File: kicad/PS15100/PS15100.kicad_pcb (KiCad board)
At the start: 2 copper layers, 22 parts

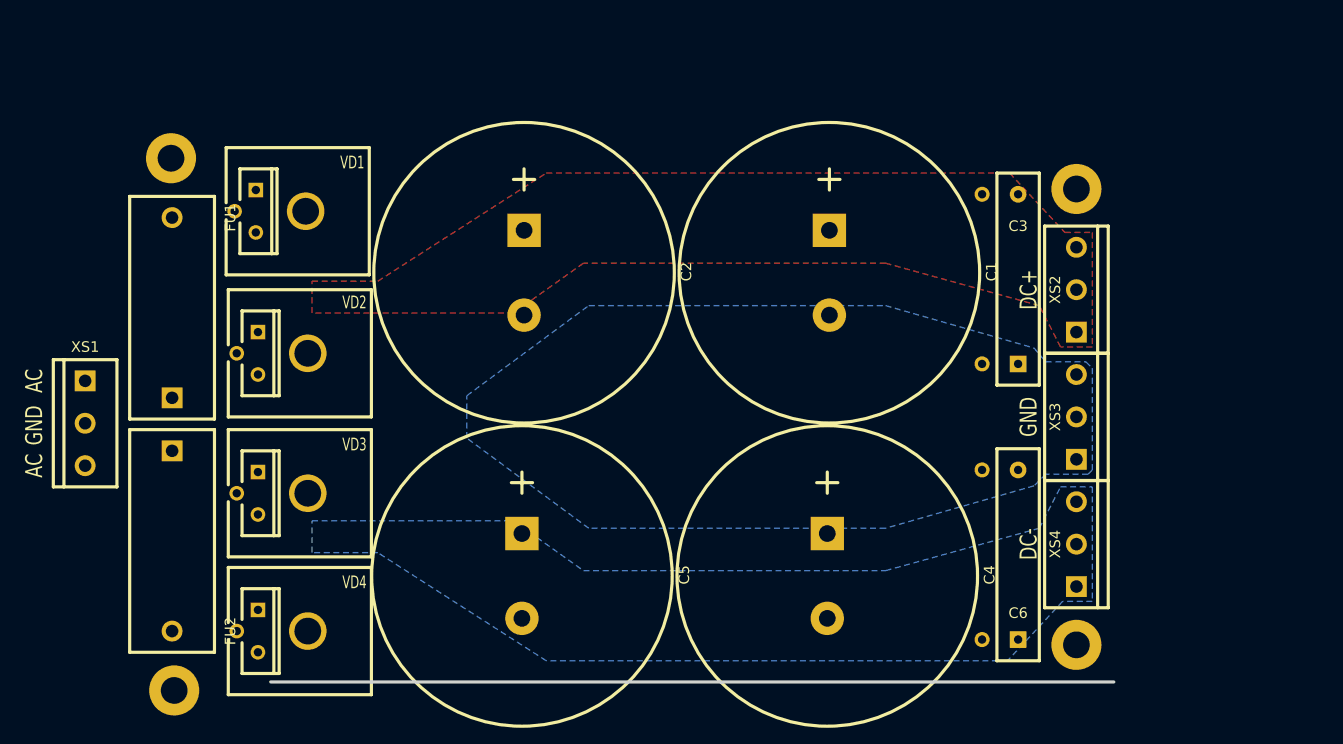
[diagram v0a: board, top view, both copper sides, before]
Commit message: Развёл плату стабилизатора на +/-100В 15А.
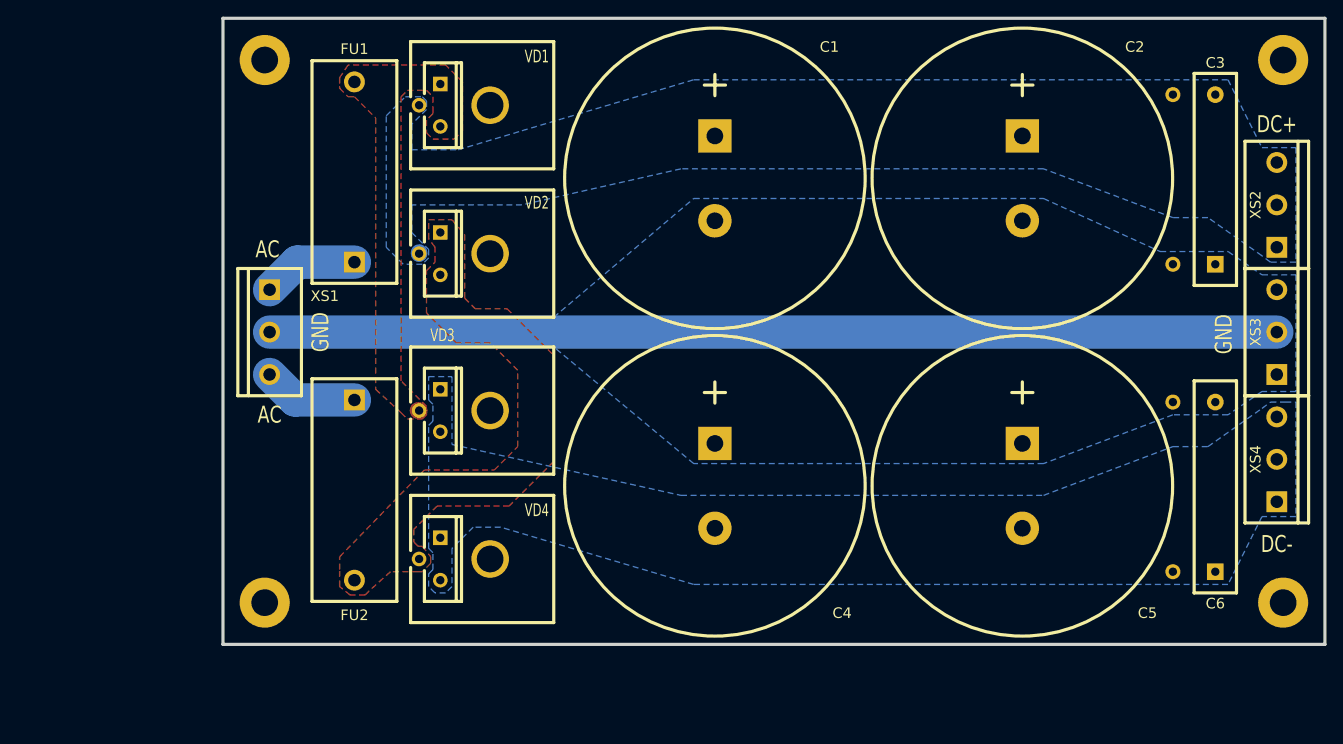
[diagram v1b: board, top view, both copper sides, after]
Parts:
- VD3: footprint LFcomponents:TO220_RAD_16.5x15_VD -> IWcomponents:TO220_RAD_16.5x15_VD
- moved C5 60.9 mm to (172.0, 104.8)
- moved C2 60.8 mm to (172.0, 67.9)
- moved FU1 27.2 mm to (91.9, 72.9)
- moved 1_PIN 27.1 mm to (206.2, 52.3)
- moved C3 26.5 mm to (195.1, 78.2)
- moved XS4 26.1 mm to (202.4, 101.6)
- moved XS2 26.1 mm to (202.4, 71.1)
- moved XS3 26.1 mm to (202.4, 86.4)
- moved R1 25.8 mm to (190.0, 68.1)
- moved VD1 25.5 mm to (108.2, 59.2)
- moved C6 25.0 mm to (195.1, 115.1)
- moved VD2 24.9 mm to (108.2, 77.0)
- moved 1_PIN 24.7 mm to (206.8, 116.8)
- moved XS1 24.6 mm to (81.8, 86.4)
- moved R2 24.3 mm to (190.0, 104.9)
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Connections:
- VD1 pad 3: (no net) -> Net-(FU1-Pad2)
- VD2 pad 3: (no net) -> Net-(FU2-Pad2)
- VD3 pad 3: (no net) -> /VCC-
- VD4 pad 3: (no net) -> /VCC-
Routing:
- net /GND: track 0.00 -> 120.6 mm
- net Net-(FU1-Pad1): track 0.00 -> 11.5 mm
- net Net-(FU2-Pad1): track 0.00 -> 11.4 mm
- added copper zone on B.Cu, net /VCC+
- added copper zone on F.Cu, net Net-(FU1-Pad2)
- added copper zone on F.Cu, net Net-(FU2-Pad2)
- removed copper zone on F.Cu, net /VCC+
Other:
- board outline added: 132 x 75 mm

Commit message: Подготовил плату PS10015 к отправке на изготовление.
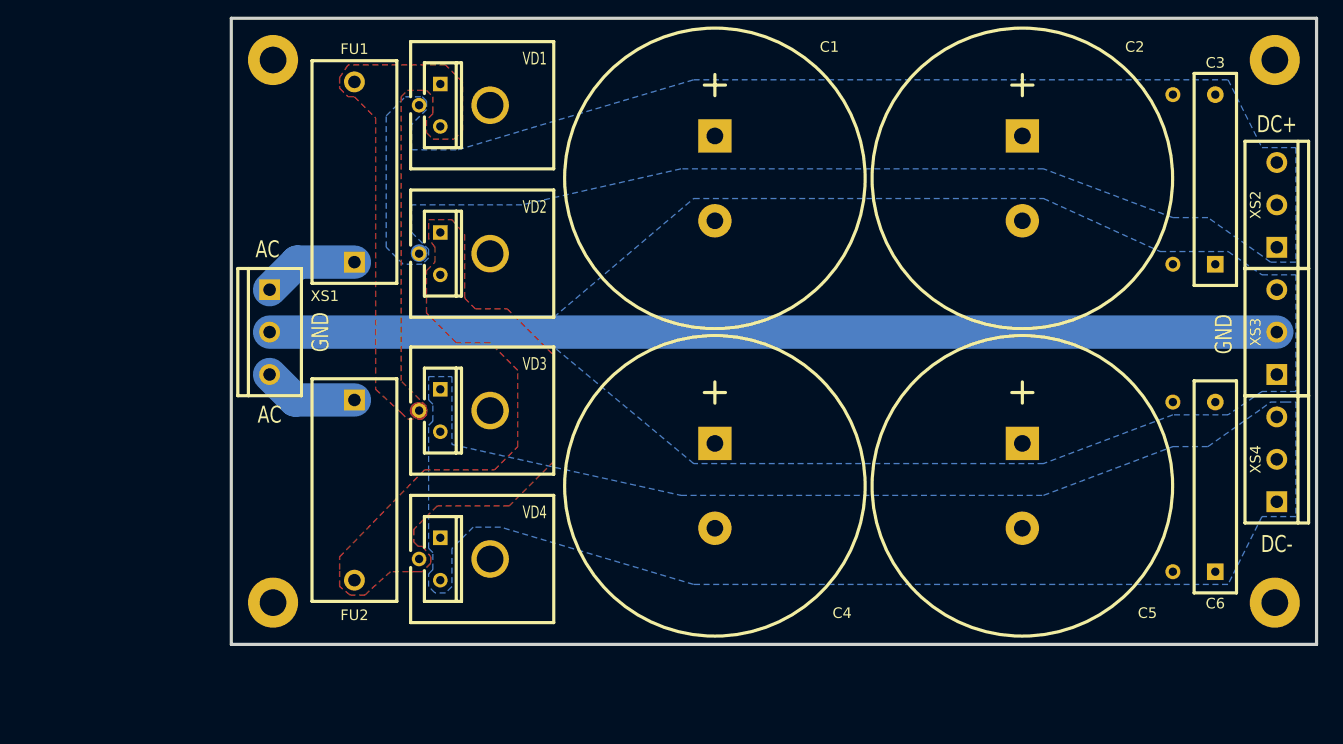
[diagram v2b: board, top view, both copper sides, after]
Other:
- board size 132 x 75 mm -> 130 x 75 mm
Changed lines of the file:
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@@
   )
   (setup
-    (last_trace_width 4)
+    (last_trace_width 1)
     (user_trace_width 2)
     (user_trace_width 4)
@@
       (usegerberextensions true)
       (excludeedgelayer true)
-      (linewidth 0.150000)
+      (linewidth 0.100000)
       (plotframeref false)
       (viasonmask false)
@@
       (plotvalue true)
       (plotinvisibletext false)
-      (padsonsilk true)
-      (subtractmaskfromsilk true)
+      (padsonsilk false)
+      (subtractmaskfromsilk false)
       (outputformat 1)
       (mirror false)
@@
       (effects (font (size 1.016 1.016) (thickness 0.254)))
     )
-    (pad 1 thru_hole circle (at -3.556 1.928) (size 6 6) (drill 3.2) (layers *.Cu *.Mask F.SilkS)
+    (pad 1 thru_hole circle (at -4.556 1.928) (size 6 6) (drill 3.2) (layers *.Cu *.Mask F.SilkS)
       (solder_mask_margin 1.99898) (clearance 1.00076))
   )
@@
       (effects (font (size 1.016 1.016) (thickness 0.254)))
     )
-    (pad 1 thru_hole circle (at -3.048 1.444) (size 6 6) (drill 3.2) (layers *.Cu *.Mask F.SilkS)
+    (pad 1 thru_hole circle (at -4.048 1.444) (size 6 6) (drill 3.2) (layers *.Cu *.Mask F.SilkS)
       (solder_mask_margin 1.99898) (clearance 1.00076))
   )
@@
       (effects (font (size 1.016 1.016) (thickness 0.254)))
     )
-    (pad 1 thru_hole circle (at 9.572 -0.612) (size 6 6) (drill 3.2) (layers *.Cu *.Mask F.SilkS)
+    (pad 1 thru_hole circle (at 10.572 -0.612) (size 6 6) (drill 3.2) (layers *.Cu *.Mask F.SilkS)
       (solder_mask_margin 1.99898) (clearance 1.00076))
   )
@@
       (effects (font (size 1.016 1.016) (thickness 0.254)))
     )
-    (pad 1 thru_hole circle (at 3.984 1.952) (size 6 6) (drill 3.2) (layers *.Cu *.Mask F.SilkS)
+    (pad 1 thru_hole circle (at 4.984 1.952) (size 6 6) (drill 3.2) (layers *.Cu *.Mask F.SilkS)
       (solder_mask_margin 1.99898) (clearance 1.00076))
   )
@@
     (at 108.204 59.182)
     (tags "TR TO220")
-    (fp_text reference VD1 (at 5.588 -5.842) (layer F.SilkS)
+    (fp_text reference VD1 (at 5.334 -5.588) (layer F.SilkS)
       (effects (font (size 1.524 1.016) (thickness 0.2032)))
     )
@@
     (at 108.204 76.962)
     (tags "TR TO220")
-    (fp_text reference VD2 (at 5.588 -6.096) (layer F.SilkS)
+    (fp_text reference VD2 (at 5.334 -5.588) (layer F.SilkS)
       (effects (font (size 1.524 1.016) (thickness 0.2032)))
     )
@@
     (at 108.204 113.538)
     (tags "TR TO220")
-    (fp_text reference VD4 (at 5.588 -5.842) (layer F.SilkS)
+    (fp_text reference VD4 (at 5.334 -5.588) (layer F.SilkS)
       (effects (font (size 1.524 1.016) (thickness 0.2032)))
     )
@@
     (at 108.204 95.758)
     (tags "TR TO220")
-    (fp_text reference VD3 (at -5.715 -9.017) (layer F.SilkS)
+    (fp_text reference VD3 (at 5.334 -5.588) (layer F.SilkS)
       (effects (font (size 1.524 1.016) (thickness 0.2032)))
     )
@@
     )
   )
-  (gr_line (start 76.2 123.768) (end 208.2 123.768) (angle 90) (layer Edge.Cuts) (width 0.381))
-  (gr_line (start 208.2 48.768) (end 208.2 123.768) (angle 90) (layer Edge.Cuts) (width 0.381))
-  (gr_line (start 76.2 48.768) (end 76.2 123.768) (angle 90) (layer Edge.Cuts) (width 0.381))
-  (gr_line (start 76.2 48.768) (end 208.2 48.768) (angle 90) (layer Edge.Cuts) (width 0.381))
+  (gr_line (start 77.2 123.768) (end 207.2 123.768) (angle 90) (layer Edge.Cuts) (width 0.381))
+  (gr_line (start 207.2 48.768) (end 207.2 123.768) (angle 90) (layer Edge.Cuts) (width 0.381))
+  (gr_line (start 77.2 48.768) (end 77.2 123.768) (angle 90) (layer Edge.Cuts) (width 0.381))
+  (gr_line (start 77.2 48.768) (end 207.2 48.768) (angle 90) (layer Edge.Cuts) (width 0.381))
   (gr_text AC (at 81.788 96.266) (layer F.SilkS)
     (effects (font (size 2.032 1.524) (thickness 0.3048)))
@@
   )
   (segment (start 81.788 86.36) (end 202.438 86.36) (width 4) (layer Back) (net 1))
-  (segment (start 99.695 76.835) (end 99.695 76.962) (width 2) (layer Back) (net 2) (status C00000))
+  (segment (start 99.695 76.835) (end 99.695 76.962) (width 2) (layer Back) (net 2))
   (segment (start 91.948 77.978) (end 85.09 77.978) (width 4) (layer Back) (net 4))
   (segment (start 85.09 77.978) (end 81.788 81.28) (width 4) (layer Back) (net 4))
-  (segment (start 99.695 95.758) (end 99.568 95.758) (width 2) (layer Front) (net 5) (status C00000))
+  (segment (start 99.695 95.758) (end 99.568 95.758) (width 2) (layer Front) (net 5))
   (segment (start 91.948 94.488) (end 84.836 94.488) (width 4) (layer Back) (net 6))
   (segment (start 84.836 94.488) (end 81.788 91.44) (width 4) (layer Back) (net 6))
